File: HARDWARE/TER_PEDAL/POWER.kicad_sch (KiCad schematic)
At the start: 13 parts, among them U2 AOZ1280CI, U3 LM1117MP-3.3

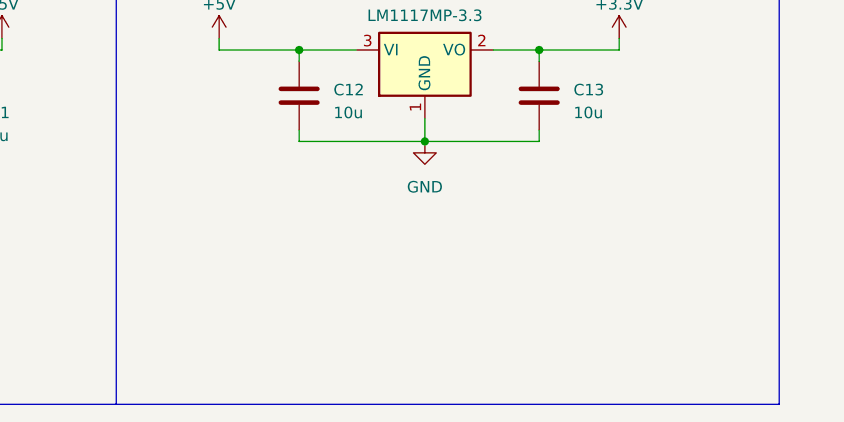
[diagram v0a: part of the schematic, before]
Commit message: Added Sensors PSU
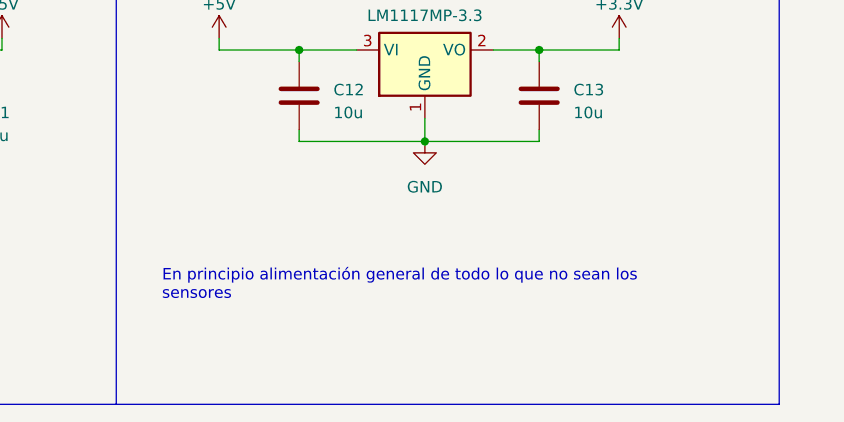
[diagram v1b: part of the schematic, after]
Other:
- note added: "En principio alimentación general de todo lo que no sean los sensores"
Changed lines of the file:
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@@
     )
+  )
+  (text "En principio alimentación general de todo lo que no sean los \nsensores"
+    (at 130.81 57.15 0)
+    (effects (font (size 1.27 1.27)) (justify left bottom))
   )
   (text "24V->5V Buck Converter (Caution Ripple)" (at 39.37 16.51 0)

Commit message: Added footprints to existing components
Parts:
- C10, C11, C12, C13: footprint (none) -> Capacitor_SMD:C_0603_1608Metric
- C9: footprint (none) -> Capacitor_SMD:C_Elec_4x5.4
- D1: footprint (none) -> Diode_SMD:D_0805_2012Metric
- F2: footprint (none) -> Fuse:Fuse_0805_2012Metric
- L1, R2: footprint (none) -> Inductor_SMD:L_6.3x6.3_H3
- R1: footprint (none) -> Connector_PinHeader_2.00mm:PinHeader_1x03_P2.00mm_Vertical
- R3: footprint (none) -> Resistor_SMD:R_0805_2012Metric
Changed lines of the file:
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@@
       (effects (font (size 1.27 1.27)) (justify left))
     )
-    (property "Footprint" "" (at 93.98 40.64 0)
+    (property "Footprint" "Resistor_SMD:R_0805_2012Metric" (at 93.98 40.64 0)
       (effects (font (size 1.27 1.27)) hide)
     )
@@
       (effects (font (size 1.27 1.27)) (justify left))
     )
-    (property "Footprint" "" (at 30.1752 39.37 0)
+    (property "Footprint" "Capacitor_SMD:C_Elec_4x5.4" (at 30.1752 39.37 0)
       (effects (font (size 1.27 1.27)) hide)
     )
@@
       (effects (font (size 1.27 1.27)) (justify left))
     )
-    (property "Footprint" "" (at 93.98 33.02 0)
+    (property "Footprint" "Inductor_SMD:L_6.3x6.3_H3" (at 93.98 33.02 0)
       (effects (font (size 1.27 1.27)) hide)
     )
@@
       (effects (font (size 1.27 1.27)) (justify left))
     )
-    (property "Footprint" "" (at 147.0152 38.1 0)
+    (property "Footprint" "Capacitor_SMD:C_0603_1608Metric" (at 147.0152 38.1 0)
       (effects (font (size 1.27 1.27)) hide)
     )
@@
       (effects (font (size 1.27 1.27)) (justify left))
     )
-    (property "Footprint" "" (at 173.6852 38.1 0)
+    (property "Footprint" "Capacitor_SMD:C_0603_1608Metric" (at 173.6852 38.1 0)
       (effects (font (size 1.27 1.27)) hide)
     )
@@
       (effects (font (size 1.27 1.27)))
     )
-    (property "Footprint" "" (at 26.67 25.4 0)
+    (property "Footprint" "Fuse:Fuse_0805_2012Metric" (at 26.67 25.4 0)
       (effects (font (size 1.27 1.27)) (justify left) hide)
     )
@@
       (effects (font (size 1.27 1.27)))
     )
-    (property "Footprint" "" (at 83.82 29.21 0)
+    (property "Footprint" "Inductor_SMD:L_6.3x6.3_H3" (at 83.82 29.21 0)
       (effects (font (size 1.27 1.27)) hide)
     )
@@
       (effects (font (size 1.27 1.27)))
     )
-    (property "Footprint" "" (at 72.39 25.7048 0)
+    (property "Footprint" "Capacitor_SMD:C_0603_1608Metric" (at 72.39 25.7048 0)
       (effects (font (size 1.27 1.27)) hide)
     )
@@
       (effects (font (size 1.27 1.27)))
     )
-    (property "Footprint" "" (at 39.37 33.528 90)
+    (property "Footprint" "Connector_PinHeader_2.00mm:PinHeader_1x03_P2.00mm_Vertical" (at 39.37 33.528 90)
       (effects (font (size 1.27 1.27)) hide)
     )
@@
       (effects (font (size 1.27 1.27)) (justify left))
     )
-    (property "Footprint" "" (at 107.6452 40.64 0)
+    (property "Footprint" "Capacitor_SMD:C_0603_1608Metric" (at 107.6452 40.64 0)
       (effects (font (size 1.27 1.27)) hide)
     )
@@
       (effects (font (size 1.27 1.27)) (justify left))
     )
-    (property "Footprint" "" (at 74.93 35.56 0)
-      (effects (font (size 1.27 1.27)) hide)
-    )
+    (property "Footprint" "Diode_SMD:D_0805_2012Metric" (at 74.93 35.56 0)
+      (effects (font (size 1.27 1.27)) hide)
+    )

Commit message: Started Layout and fixed wrong footprints
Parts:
- R1: footprint Connector_PinHeader_2.00mm:PinHeader_1x03_P2.00mm_Vertical -> Resistor_SMD:R_0603_1608Metric
- R2: footprint Inductor_SMD:L_6.3x6.3_H3 -> Resistor_SMD:R_0603_1608Metric
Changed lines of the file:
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@@
       (effects (font (size 1.27 1.27)) (justify left))
     )
-    (property "Footprint" "Inductor_SMD:L_6.3x6.3_H3" (at 93.98 33.02 0)
+    (property "Footprint" "Resistor_SMD:R_0603_1608Metric" (at 93.98 33.02 0)
       (effects (font (size 1.27 1.27)) hide)
     )
@@
       (effects (font (size 1.27 1.27)))
     )
-    (property "Footprint" "Connector_PinHeader_2.00mm:PinHeader_1x03_P2.00mm_Vertical" (at 39.37 33.528 90)
-      (effects (font (size 1.27 1.27)) hide)
-    )
+    (property "Footprint" "Resistor_SMD:R_0603_1608Metric" (at 39.37 33.528 90)
+      (effects (font (size 1.27 1.27)) hide)
+    )

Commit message: Sized and Fixed even more footprints + Initial layout
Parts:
- C11: footprint Capacitor_SMD:C_0603_1608Metric -> Capacitor_SMD:C_1210_3225Metric
- C9: footprint Capacitor_SMD:C_Elec_4x5.4 -> Capacitor_SMD:C_1210_3225Metric
- L1: footprint Inductor_SMD:L_6.3x6.3_H3 -> Inductor_SMD_Wurth:L_Wurth_WE-LQSH-4020
- R3: footprint Resistor_SMD:R_0805_2012Metric -> Resistor_SMD:R_0603_1608Metric
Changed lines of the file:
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@@
       (effects (font (size 1.27 1.27)) (justify left))
     )
-    (property "Footprint" "Resistor_SMD:R_0805_2012Metric" (at 93.98 40.64 0)
+    (property "Footprint" "Resistor_SMD:R_0603_1608Metric" (at 93.98 40.64 0)
       (effects (font (size 1.27 1.27)) hide)
     )
@@
       (effects (font (size 1.27 1.27)) (justify left))
     )
-    (property "Footprint" "Capacitor_SMD:C_Elec_4x5.4" (at 30.1752 39.37 0)
+    (property "Footprint" "Capacitor_SMD:C_1210_3225Metric" (at 30.1752 39.37 0)
       (effects (font (size 1.27 1.27)) hide)
     )
@@
       (effects (font (size 1.27 1.27)))
     )
-    (property "Footprint" "Inductor_SMD:L_6.3x6.3_H3" (at 83.82 29.21 0)
+    (property "Footprint" "Inductor_SMD_Wurth:L_Wurth_WE-LQSH-4020" (at 83.82 29.21 0)
       (effects (font (size 1.27 1.27)) hide)
     )
@@
       (effects (font (size 1.27 1.27)) (justify left))
     )
-    (property "Footprint" "Capacitor_SMD:C_0603_1608Metric" (at 107.6452 40.64 0)
-      (effects (font (size 1.27 1.27)) hide)
-    )
+    (property "Footprint" "Capacitor_SMD:C_1210_3225Metric" (at 107.6452 40.64 0)
+      (effects (font (size 1.27 1.27)) hide)
+    )

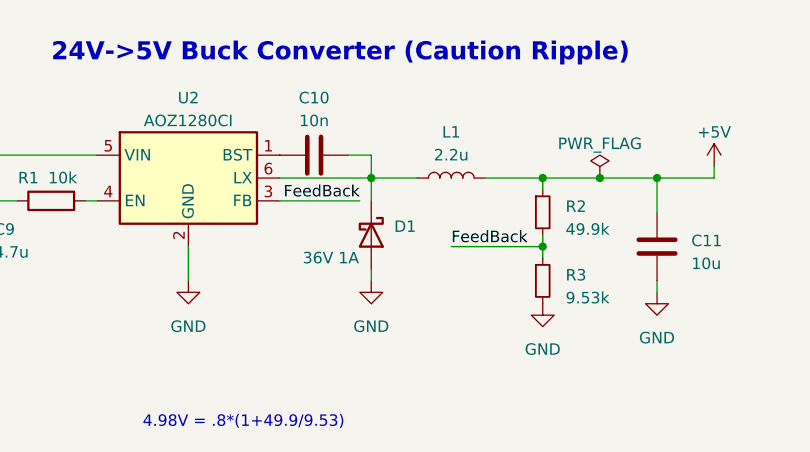
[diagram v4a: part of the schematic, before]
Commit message: Began layout and switched to 4 layer board
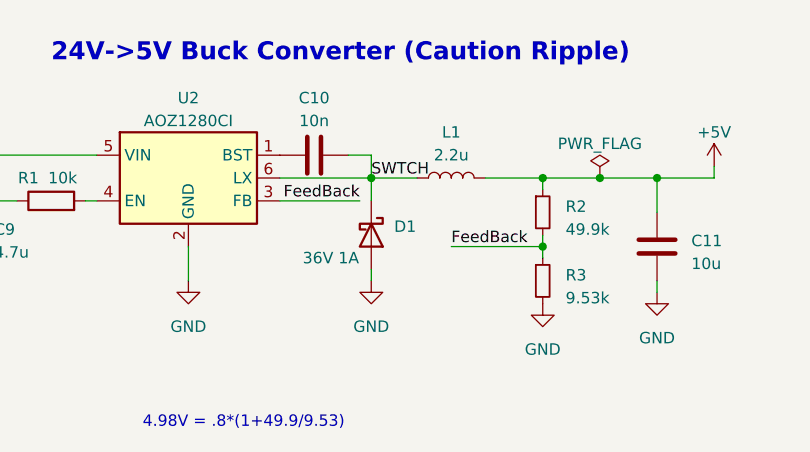
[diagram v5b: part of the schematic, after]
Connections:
- net SWTCH: now reaches C10.2, D1.1 (K), L1.1, U2.6 (LX)
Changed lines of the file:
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@@
+    (effects (font (size 1.27 1.27)) (justify left bottom))
+  )
+  (label "SWTCH" (at 74.93 29.21 0) (fields_autoplaced)
     (effects (font (size 1.27 1.27)) (justify left bottom))
   )

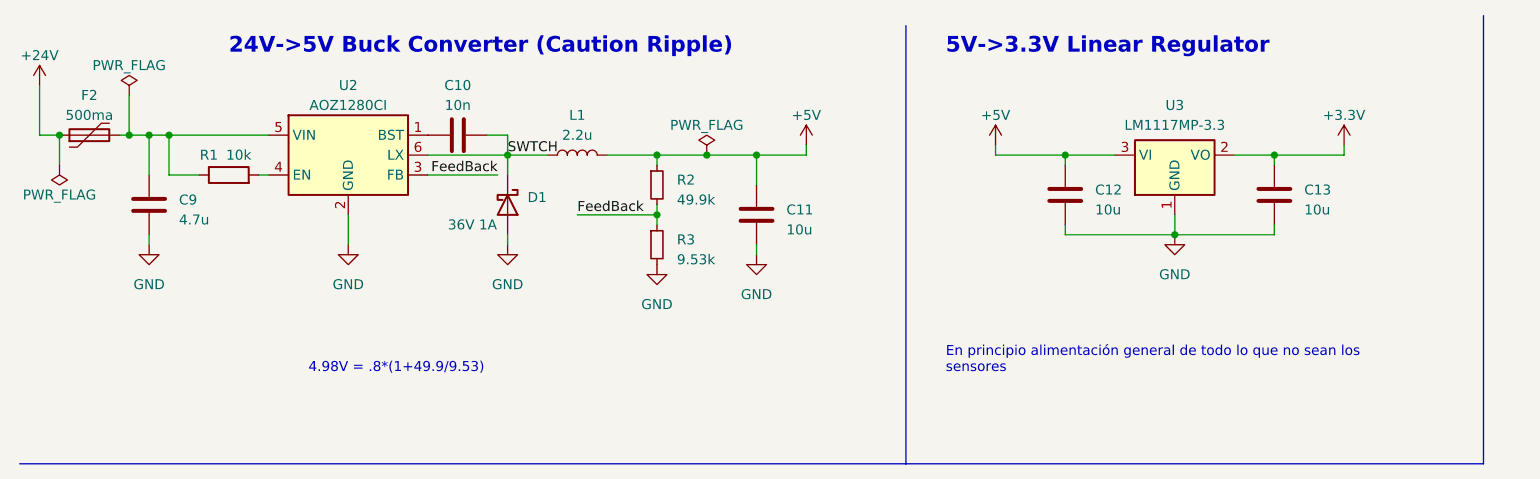
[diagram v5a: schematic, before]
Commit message: Swapped Custom Supply for traco for simplicity
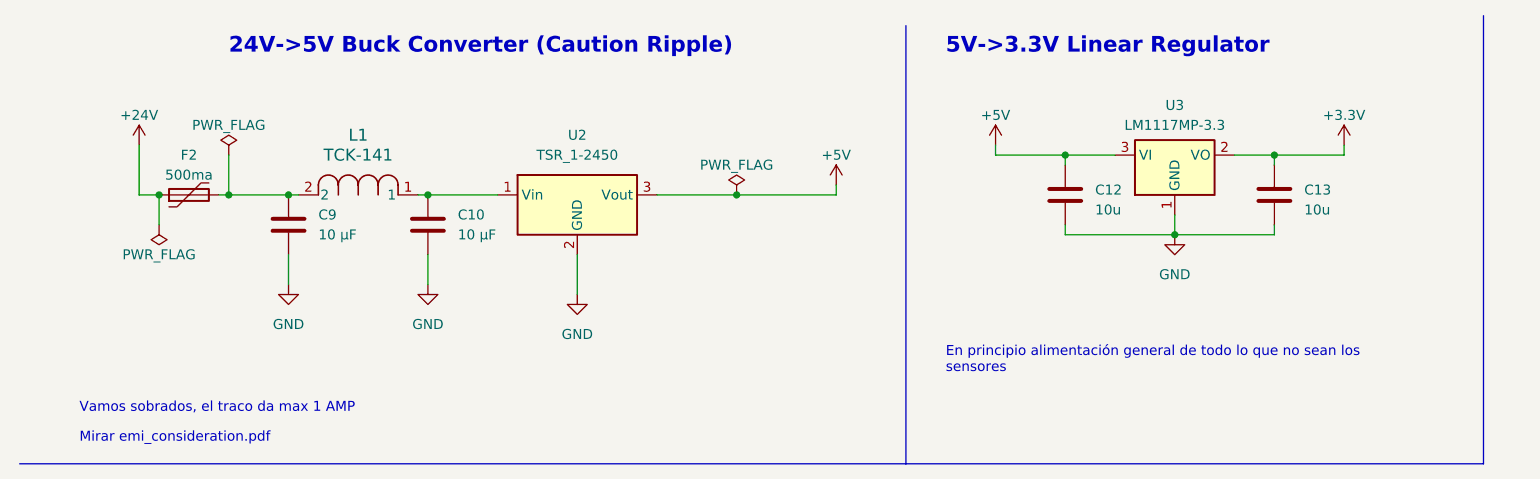
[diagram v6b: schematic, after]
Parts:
- removed C11: 10u, Capacitor_SMD:C_1210_3225Metric, symbol Device:C
- removed D1: 36V 1A, Diode_SMD:D_0805_2012Metric, symbol Device:D_Schottky
- removed L1: 2.2u, Inductor_SMD_Wurth:L_Wurth_WE-LQSH-4020, symbol Device:L
- removed R1: 10k, Resistor_SMD:R_0603_1608Metric, symbol Device:R
- removed R2: 49.9k, Resistor_SMD:R_0603_1608Metric, symbol Device:R_Small
- removed R3: 9.53k, Resistor_SMD:R_0603_1608Metric, symbol Device:R_Small
- removed U2: AOZ1280CI, Package_TO_SOT_SMD:SOT-23-6, symbol Regulator_Switching:AOZ1280CI
- added L1: TCK-141, Footprints:IND_TCK-141_TRP, symbol TracoChoke:TCK-141
- added U2: TSR_1-2450, Converter_DCDC:Converter_DCDC_TRACO_TSR-1_THT, symbol Regulator_Switching:TSR_1-2450
- C10: value 10n -> 10 µF; footprint Capacitor_SMD:C_0603_1608Metric -> Capacitor_SMD:C_0805_2012Metric
- C9: value 4.7u -> 10 µF; footprint Capacitor_SMD:C_1210_3225Metric -> Capacitor_SMD:C_0805_2012Metric
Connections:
- net SWTCH is gone; now on net GND: C10.2
- net +5V: now also U2.3 (Vout)
- net GND: now also U2.2 (GND)
- net at C9.1, F2.2: now also L1.2
- net at C10.1: now also L1.1, U2.1 (Vin)
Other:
- note added: "Mirar emi_consideration.pdf"
- note added: "Vamos sobrados, el traco da max 1 AMP"
- note removed: "4.98V = .8*(1+49.9/9.53)"
- moved on the sheet: F2

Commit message: Added voltage followers to sensing, improved can circuitri, improved layout, waiting for routing
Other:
- company: (none) -> Tecnun-eRacing
- title: (none) -> TeR_PEDAL
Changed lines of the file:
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@@
 	(generator_version "8.0")
 	(paper "A4")
+	(title_block
+		(title "TeR_PEDAL")
+		(date "2023-11-24")
+		(rev "V1.1.0")
+		(company "Tecnun-eRacing")
+		(comment 1 "Ozuba")
+	)
 	(junction
 		(at 104.14 34.29)
